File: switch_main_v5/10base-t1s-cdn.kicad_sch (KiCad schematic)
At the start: 11 parts, among them T2101 74930100

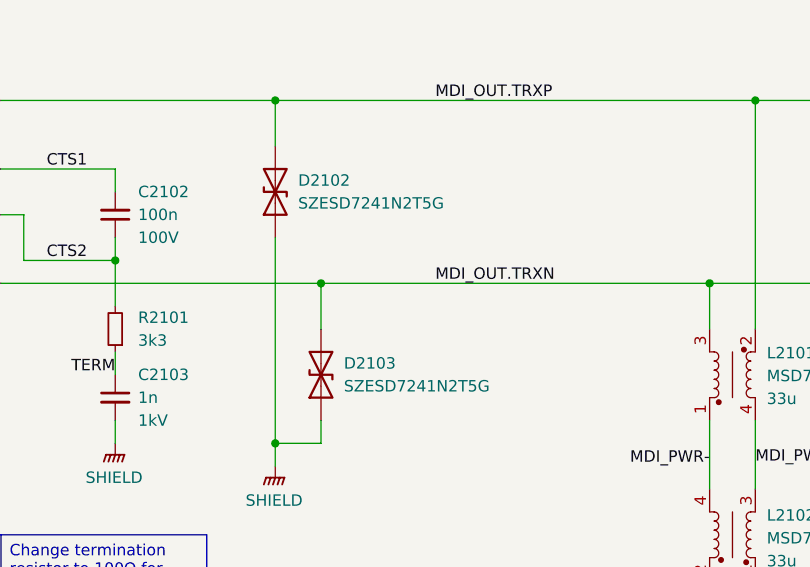
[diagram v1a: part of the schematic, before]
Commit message: Changed main 3V3 regulator to 3A, added switch 2 crystal & other changes
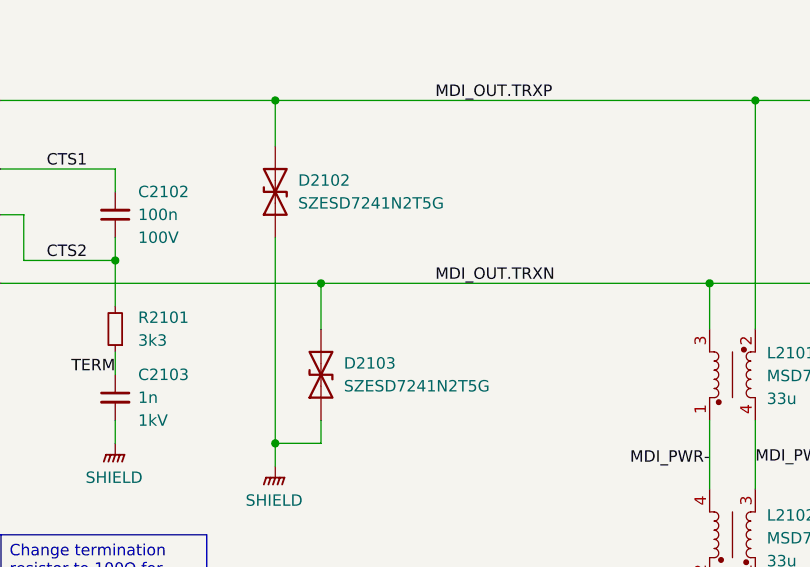
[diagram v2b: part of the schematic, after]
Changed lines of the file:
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@@
 	(symbol
 		(lib_id "TVS:SZESD7241N2T5G")
-		(at 177.8 124.46 90)
+		(at 180.34 124.46 90)
 		(unit 1)
 		(exclude_from_sim no)
@@
 		(on_board yes)
 		(dnp no)
-		(fields_autoplaced yes)
 		(property "Reference" "D2103"
-			(at 182.88 123.1899 90)
+			(at 182.88 123.19 90)
 			(effects
 				(font
@@
 		)
 		(property "Value" "SZESD7241N2T5G"
-			(at 182.88 125.7299 90)
+			(at 182.88 125.73 90)
 			(effects
 				(font
@@
 		)
 		(property "Footprint" "project_footprints:SZESD7462N2T5G"
-			(at 187.96 140.97 0)
+			(at 190.5 140.97 0)
 			(effects
 				(font
@@
 		)
 		(property "Datasheet" "https://www.onsemi.com/pub/Collateral/ESD7241-D.PDF"
-			(at 190.5 153.67 0)
+			(at 193.04 153.67 0)
 			(effects
 				(font
@@
 		)
 		(property "Description" "SZESD7241MXWT5G Wettable Flank Package; SZ Prefix for Automotive and Other Applications Requiring Unique Site and Control Change Requirements; AECQ101 Qualified and PPAP CapableSZ Prefix for Automotive and Other Applications Requiring Unique Site and Control Change Requirements; AECQ101 Qualified and PPAP Capable; Ultra-Low Capacitance: < 1.0pF Max; Low Leakage: < 0.5uA; IEC61000-4-2 (ESD): Level 4 +/-28kV Contact; IEC61000-4-4 (EFT): 40A - 5/50ns; IEC61000-4-5 (Lightning): 1A - 8/20us; These Devices are Pb"
-			(at 184.15 124.46 0)
+			(at 186.69 124.46 0)
 			(effects
 				(font
@@
 		)
 		(property "Height" "0.4"
-			(at 193.04 125.73 0)
+			(at 195.58 125.73 0)
 			(effects
 				(font
@@
 		)
 		(property "Mouser Part Number" "863-SZESD7241N2T5G"
-			(at 195.58 135.89 0)
+			(at 198.12 135.89 0)
 			(effects
 				(font
@@
 		)
 		(property "Mouser Price/Stock" "https://www.mouser.co.uk/ProductDetail/onsemi/SZESD7241N2T5G?qs=z6PAvqrnkvSq0oMCl81g4Q%3D%3D"
-			(at 198.12 173.99 0)
+			(at 200.66 173.99 0)
 			(effects
 				(font
@@
 		)
 		(property "Manufacturer_Name" "onsemi"
-			(at 200.66 128.27 0)
+			(at 203.2 128.27 0)
 			(effects
 				(font
@@
 		)
 		(property "Manufacturer_Part_Number" "SZESD7241N2T5G"
-			(at 203.2 133.35 0)
+			(at 205.74 133.35 0)
 			(effects
 				(font
@@
 	(symbol
 		(lib_id "TVS:SZESD7241N2T5G")
-		(at 172.72 104.14 90)
+		(at 175.26 104.14 90)
 		(unit 1)
 		(exclude_from_sim no)
@@
 		(dnp no)
 		(property "Reference" "D2102"
-			(at 177.8 102.8699 90)
+			(at 177.8 102.87 90)
 			(effects
 				(font
@@
 		)
 		(property "Value" "SZESD7241N2T5G"
-			(at 177.8 105.4099 90)
+			(at 177.8 105.41 90)
 			(effects
 				(font
@@
 		)
 		(property "Footprint" "project_footprints:SZESD7462N2T5G"
-			(at 182.88 120.65 0)
+			(at 185.42 120.65 0)
 			(effects
 				(font
@@
 		)
 		(property "Datasheet" "https://www.onsemi.com/pub/Collateral/ESD7241-D.PDF"
-			(at 185.42 133.35 0)
+			(at 187.96 133.35 0)
 			(effects
 				(font
@@
 		)
 		(property "Description" "SZESD7241MXWT5G Wettable Flank Package; SZ Prefix for Automotive and Other Applications Requiring Unique Site and Control Change Requirements; AECQ101 Qualified and PPAP CapableSZ Prefix for Automotive and Other Applications Requiring Unique Site and Control Change Requirements; AECQ101 Qualified and PPAP Capable; Ultra-Low Capacitance: < 1.0pF Max; Low Leakage: < 0.5uA; IEC61000-4-2 (ESD): Level 4 +/-28kV Contact; IEC61000-4-4 (EFT): 40A - 5/50ns; IEC61000-4-5 (Lightning): 1A - 8/20us; These Devices are Pb"
-			(at 179.07 104.14 0)
+			(at 181.61 104.14 0)
 			(effects
 				(font
@@
 		)
 		(property "Height" "0.4"
-			(at 187.96 105.41 0)
+			(at 190.5 105.41 0)
 			(effects
 				(font
@@
 		)
 		(property "Mouser Part Number" "863-SZESD7241N2T5G"
-			(at 190.5 115.57 0)
+			(at 193.04 115.57 0)
 			(effects
 				(font
@@
 		)
 		(property "Mouser Price/Stock" "https://www.mouser.co.uk/ProductDetail/onsemi/SZESD7241N2T5G?qs=z6PAvqrnkvSq0oMCl81g4Q%3D%3D"
-			(at 193.04 153.67 0)
+			(at 195.58 153.67 0)
 			(effects
 				(font
@@
 		)
 		(property "Manufacturer_Name" "onsemi"
-			(at 195.58 107.95 0)
+			(at 198.12 107.95 0)
 			(effects
 				(font
@@
 		)
 		(property "Manufacturer_Part_Number" "SZESD7241N2T5G"
-			(at 198.12 113.03 0)
-			(effects
-				(font
+			(at 200.66 113.03 0)
+			(effects
+				(font

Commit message: Tidied schematic and PCB
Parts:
- renumbered C2102 to C2901, C2101 to C2902, C2103 to C2903, D2102 to D2901, D2101 to D2902, D2103 to D2903, FL2101 to FL2901, L2101 to L2901, L2102 to L2902, R2101 to R2901, T2101 to T2901
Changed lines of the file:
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@@
 		(on_board yes)
 		(dnp no)
-		(property "Reference" "C2101"
+		(property "Reference" "C2902"
 			(at 119.38 115.5762 0)
 			(effects
@@
 			(project "switch_main_v4"
 				(path "/a5e57332-4284-4d3c-ab3c-13bc0ddb29b6/1d1a9833-050c-427e-aa22-8f19cbf4f64e/c4e1641a-ba0e-4849-bfcb-134e004c6188"
-					(reference "C2101")
+					(reference "C2902")
 					(unit 1)
 				)
@@
 		(dnp no)
 		(fields_autoplaced yes)
-		(property "Reference" "D2101"
+		(property "Reference" "D2902"
 			(at 60.96 111.76 0)
 			(effects
@@
 			(project "switch_main_v4"
 				(path "/a5e57332-4284-4d3c-ab3c-13bc0ddb29b6/1d1a9833-050c-427e-aa22-8f19cbf4f64e/c4e1641a-ba0e-4849-bfcb-134e004c6188"
-					(reference "D2101")
+					(reference "D2902")
 					(unit 1)
 				)
@@
 		(dnp no)
 		(fields_autoplaced yes)
-		(property "Reference" "#PWR02105"
+		(property "Reference" "#PWR02905"
 			(at 175.26 139.7 0)
 			(effects
@@
 			(project "switch_main_v4"
 				(path "/a5e57332-4284-4d3c-ab3c-13bc0ddb29b6/1d1a9833-050c-427e-aa22-8f19cbf4f64e/c4e1641a-ba0e-4849-bfcb-134e004c6188"
-					(reference "#PWR02105")
+					(reference "#PWR02905")
 					(unit 1)
 				)
@@
 		(dnp no)
 		(fields_autoplaced yes)
-		(property "Reference" "#PWR02102"
+		(property "Reference" "#PWR02903"
 			(at 73.66 138.43 0)
 			(effects
@@
 			(project "switch_main_v4"
 				(path "/a5e57332-4284-4d3c-ab3c-13bc0ddb29b6/1d1a9833-050c-427e-aa22-8f19cbf4f64e/c4e1641a-ba0e-4849-bfcb-134e004c6188"
-					(reference "#PWR02102")
+					(reference "#PWR02903")
 					(unit 1)
 				)
@@
 		(on_board yes)
 		(dnp no)
-		(property "Reference" "L2101"
+		(property "Reference" "L2901"
 			(at 229.87 122.0469 90)
 			(effects
@@
 			(project "switch_main_v4"
 				(path "/a5e57332-4284-4d3c-ab3c-13bc0ddb29b6/1d1a9833-050c-427e-aa22-8f19cbf4f64e/c4e1641a-ba0e-4849-bfcb-134e004c6188"
-					(reference "L2101")
+					(reference "L2901")
 					(unit 1)
 				)
@@
 		(on_board yes)
 		(dnp no)
-		(property "Reference" "D2103"
+		(property "Reference" "D2903"
 			(at 182.88 123.19 90)
 			(effects
@@
 			(project "switch_main_v4"
 				(path "/a5e57332-4284-4d3c-ab3c-13bc0ddb29b6/1d1a9833-050c-427e-aa22-8f19cbf4f64e/c4e1641a-ba0e-4849-bfcb-134e004c6188"
-					(reference "D2103")
+					(reference "D2903")
 					(unit 1)
 				)
@@
 		(dnp no)
 		(fields_autoplaced yes)
-		(property "Reference" "R2101"
+		(property "Reference" "R2901"
 			(at 160.02 118.1099 0)
 			(effects
@@
 			(project "switch_main_v4"
 				(path "/a5e57332-4284-4d3c-ab3c-13bc0ddb29b6/1d1a9833-050c-427e-aa22-8f19cbf4f64e/c4e1641a-ba0e-4849-bfcb-134e004c6188"
-					(reference "R2101")
+					(reference "R2901")
 					(unit 1)
 				)
@@
 		(dnp no)
 		(fields_autoplaced yes)
-		(property "Reference" "L2102"
+		(property "Reference" "L2902"
 			(at 229.87 140.0809 90)
 			(effects
@@
 			(project "switch_main_v4"
 				(path "/a5e57332-4284-4d3c-ab3c-13bc0ddb29b6/1d1a9833-050c-427e-aa22-8f19cbf4f64e/c4e1641a-ba0e-4849-bfcb-134e004c6188"
-					(reference "L2102")
+					(reference "L2902")
 					(unit 1)
 				)
@@
 		(on_board yes)
 		(dnp no)
-		(property "Reference" "C2102"
+		(property "Reference" "C2901"
 			(at 160.02 104.14 0)
 			(effects
@@
 			(project "switch_main_v4"
 				(path "/a5e57332-4284-4d3c-ab3c-13bc0ddb29b6/1d1a9833-050c-427e-aa22-8f19cbf4f64e/c4e1641a-ba0e-4849-bfcb-134e004c6188"
-					(reference "C2102")
+					(reference "C2901")
 					(unit 1)
 				)
@@
 		(dnp no)
 		(fields_autoplaced yes)
-		(property "Reference" "#PWR02103"
+		(property "Reference" "#PWR02901"
 			(at 116.84 128.27 0)
 			(effects
@@
 			(project "switch_main_v4"
 				(path "/a5e57332-4284-4d3c-ab3c-13bc0ddb29b6/1d1a9833-050c-427e-aa22-8f19cbf4f64e/c4e1641a-ba0e-4849-bfcb-134e004c6188"
-					(reference "#PWR02103")
+					(reference "#PWR02901")
 					(unit 1)
 				)
@@
 		(on_board yes)
 		(dnp no)
-		(property "Reference" "D2102"
+		(property "Reference" "D2901"
 			(at 177.8 102.87 90)
 			(effects
@@
 			(project "switch_main_v4"
 				(path "/a5e57332-4284-4d3c-ab3c-13bc0ddb29b6/1d1a9833-050c-427e-aa22-8f19cbf4f64e/c4e1641a-ba0e-4849-bfcb-134e004c6188"
-					(reference "D2102")
+					(reference "D2901")
 					(unit 1)
 				)
@@
 		(on_board yes)
 		(dnp no)
-		(property "Reference" "FL2101"
+		(property "Reference" "FL2901"
 			(at 83.82 92.71 0)
 			(effects
@@
 			(project ""
 				(path "/a5e57332-4284-4d3c-ab3c-13bc0ddb29b6/1d1a9833-050c-427e-aa22-8f19cbf4f64e/c4e1641a-ba0e-4849-bfcb-134e004c6188"
-					(reference "FL2101")
+					(reference "FL2901")
 					(unit 1)
 				)
@@
 		(dnp no)
 		(fields_autoplaced yes)
-		(property "Reference" "#PWR02101"
+		(property "Reference" "#PWR02902"
 			(at 48.26 138.43 0)
 			(effects
@@
 			(project "switch_main_v4"
 				(path "/a5e57332-4284-4d3c-ab3c-13bc0ddb29b6/1d1a9833-050c-427e-aa22-8f19cbf4f64e/c4e1641a-ba0e-4849-bfcb-134e004c6188"
-					(reference "#PWR02101")
+					(reference "#PWR02902")
 					(unit 1)
 				)
@@
 		(dnp no)
 		(fields_autoplaced yes)
-		(property "Reference" "T2101"
+		(property "Reference" "T2901"
 			(at 134.62 88.9 0)
 			(effects
@@
 			(project "switch_main_v4"
 				(path "/a5e57332-4284-4d3c-ab3c-13bc0ddb29b6/1d1a9833-050c-427e-aa22-8f19cbf4f64e/c4e1641a-ba0e-4849-bfcb-134e004c6188"
-					(reference "T2101")
+					(reference "T2901")
 					(unit 1)
 				)
@@
 		(dnp no)
 		(fields_autoplaced yes)
-		(property "Reference" "#PWR02104"
+		(property "Reference" "#PWR02904"
 			(at 157.48 137.16 0)
 			(effects
@@
 			(project "switch_main_v4"
 				(path "/a5e57332-4284-4d3c-ab3c-13bc0ddb29b6/1d1a9833-050c-427e-aa22-8f19cbf4f64e/c4e1641a-ba0e-4849-bfcb-134e004c6188"
-					(reference "#PWR02104")
+					(reference "#PWR02904")
 					(unit 1)
 				)
@@
 		(on_board yes)
 		(dnp no)
-		(property "Reference" "C2103"
+		(property "Reference" "C2903"
 			(at 160.02 124.46 0)
 			(effects
@@
 			(project "switch_main_v4"
 				(path "/a5e57332-4284-4d3c-ab3c-13bc0ddb29b6/1d1a9833-050c-427e-aa22-8f19cbf4f64e/c4e1641a-ba0e-4849-bfcb-134e004c6188"
-					(reference "C2103")
-					(unit 1)
-				)
+					(reference "C2903")
+					(unit 1)
+				)
